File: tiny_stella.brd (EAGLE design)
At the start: 99.7 x 85.1 mm, 73 parts, among them SW1 RGT_DIFFICULTY, SW2 LFT_DIFFICULTY, SW3 ON/OFF, T1 2N3904, T2 PN3906, T3 PN3906, X1 SSW-112-02-G-Q

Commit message: labeled everything and started laying traces
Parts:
- S3, S4: device SparkFun-Switches:TACTILE_SWITCH_SMD_6.0X3.5MM -> SparkFun-Switches:TACTILE_SWITCH_PTH_6.0MM_KIT
- moved JP1 7.34 mm to (71.4, 64.9)
- moved R11 6.40 mm to (36.3, 38.4), flipped to the bottom, turned to 0 degrees
- moved R10 6.14 mm to (36.3, 36.1), flipped to the bottom, turned to 0 degrees
- moved C1 5.89 mm to (36.3, 33.8), flipped to the bottom
- moved R5 5.64 mm to (36.3, 31.5), flipped to the bottom
- moved R4 5.39 mm to (36.3, 29.2), flipped to the bottom
- moved R3 5.14 mm to (36.3, 26.9), flipped to the bottom, turned to 0 degrees
- moved R8 5.14 mm to (36.3, 24.4), flipped to the bottom, turned to 0 degrees
- moved R2 4.58 mm to (31.8, 26.9), flipped to the bottom, turned to 0 degrees
- moved R7 4.58 mm to (31.8, 24.4), flipped to the bottom, turned to 0 degrees
- moved R20 4.06 mm to (45.7, 10.2), flipped to the bottom, turned to 0 degrees
- moved SW1 3.87 mm to (56.9, 74.9), turned to 90 degrees
- moved SW2 3.87 mm to (56.9, 69.8), turned to 270 degrees
- moved R1 3.81 mm to (31.8, 19.3), flipped to the bottom, turned to 0 degrees
- moved R6 3.81 mm to (31.8, 16.8), flipped to the bottom, turned to 0 degrees
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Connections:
- net GND: now also S3.3, S4.3; no longer S3.2, S4.2
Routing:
- net N$8: track 0.00 -> 28.3 mm
- net N$17: track 0.00 -> 25.2 mm
- net N$25: track 0.00 -> 22.4 mm
- net +5V: track 0.00 -> 17.9 mm, vias 0 -> 2
- net N$14: track 0.00 -> 16.6 mm
- net N$4: track 0.00 -> 16.2 mm, vias 0 -> 1
- net N$5: track 0.00 -> 15.2 mm, vias 0 -> 1
- net N$16: track 0.00 -> 14.1 mm, vias 0 -> 2
- net N$3: track 0.00 -> 12.7 mm, vias 0 -> 1
- net N$15: track 0.00 -> 6.70 mm
- net N$13: track 0.00 -> 6.37 mm
- net N$2: track 0.00 -> 6.04 mm
- net N$1: track 0.00 -> 6.04 mm
- net N$6: track 0.00 -> 4.57 mm
- net N$24: track 0.00 -> 3.97 mm
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- added copper zone on layer 1, net GND
- added copper zone on layer 16, net GND
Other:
- board text added: "+5V"
- board text added: "A10"
- board text added: "A11"
- board text added: "A12"
- board text added: "A6"
- board text added: "A7"
- board text added: "A8"
- board text added: "A9"
- board text added: "AU1"
- board text added: "AU2"
- board text added: "AUDIO"
- board text added: "BLK"
- board text added: "BUTTONS"
- board text added: "BW/ COLOR"
- board text added: "CLK"
- board text added: "COL"
- board text added: "D1"
- board text added: "D2"
- board text added: "D3"
- board text added: "D4"
- board text added: "D5"
- board text added: "D6"
- board text added: "D7"
- board text added: "D8"
- board text added: "DATA BUS"
- board text added: "DEL"
- board text added: "IRQ"
- board text added: "LEFT FIRE"
- board text added: "LEFT PADDLE A"
- board text added: "LEFT PADDLE B"
- board text added: "LM0"
- board text added: "LM1"
- board text added: "LM2"
- board text added: "PADDLES"
- board text added: "PB2"
- board text added: "PHI0"
- board text added: "PHI2"
- board text added: "R/W"
- board text added: "RDY"
- board text added: "RES"
- board text added: "RIGHT FIRE"
- board text added: "RIGHT PADDLE A"
- board text added: "RIGHT PADDLE B"
- board text added: "SELECT"
- board text added: "SHORT T0 RESET"
- board text added: "START"
- board text added: "SYNC"
- board text added: "VIDEO"

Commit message: more traces
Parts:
- moved C10 81.3 mm to (73.4, 57.4), turned to 0 degrees
- moved C5 11.4 mm to (6.35, 32.8), turned to 90 degrees
- moved C9 9.15 mm to (28.2, 69.1), turned to 180 degrees
- moved R30 8.92 mm to (6.10, 51.3), turned to 270 degrees
- moved C14 5.47 mm to (40.4, 68.3), turned to 0 degrees
- moved R29 4.83 mm to (2.29, 46.7)
- moved T3 4.58 mm to (2.54, 42.4)
- moved C19 2.81 mm to (2.29, 51.3), turned to 90 degrees
- moved R15 2.79 mm to (3.05, 22.1)
- moved X1 1.52 mm to (53.0, 59.3)
- moved C8 0.25 mm to (24.1, 69.1), turned to 0 degrees
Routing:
- net A0: track 0.00 -> 58.5 mm
- net A1: track 0.00 -> 56.0 mm
- net A2: track 0.00 -> 53.5 mm, vias 0 -> 2
- net A3: track 0.00 -> 51.8 mm
- net RGT_JOY_UP: track 0.00 -> 48.6 mm
- net A4: track 0.00 -> 47.5 mm
- net RGT_JOY_DWN: track 0.00 -> 44.2 mm
- net A5: track 0.00 -> 41.0 mm
- net RGT_JOY_LFT: track 0.00 -> 40.5 mm
- net +5V: track 17.9 -> 58.3 mm
- net RGT_JOY_RGT: track 0.00 -> 38.1 mm
- net N$32: track 0.00 -> 33.4 mm
- net N$27: track 0.00 -> 16.3 mm
- net N$31: track 0.00 -> 13.7 mm
- net N$33: track 0.00 -> 11.6 mm, vias 0 -> 2
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
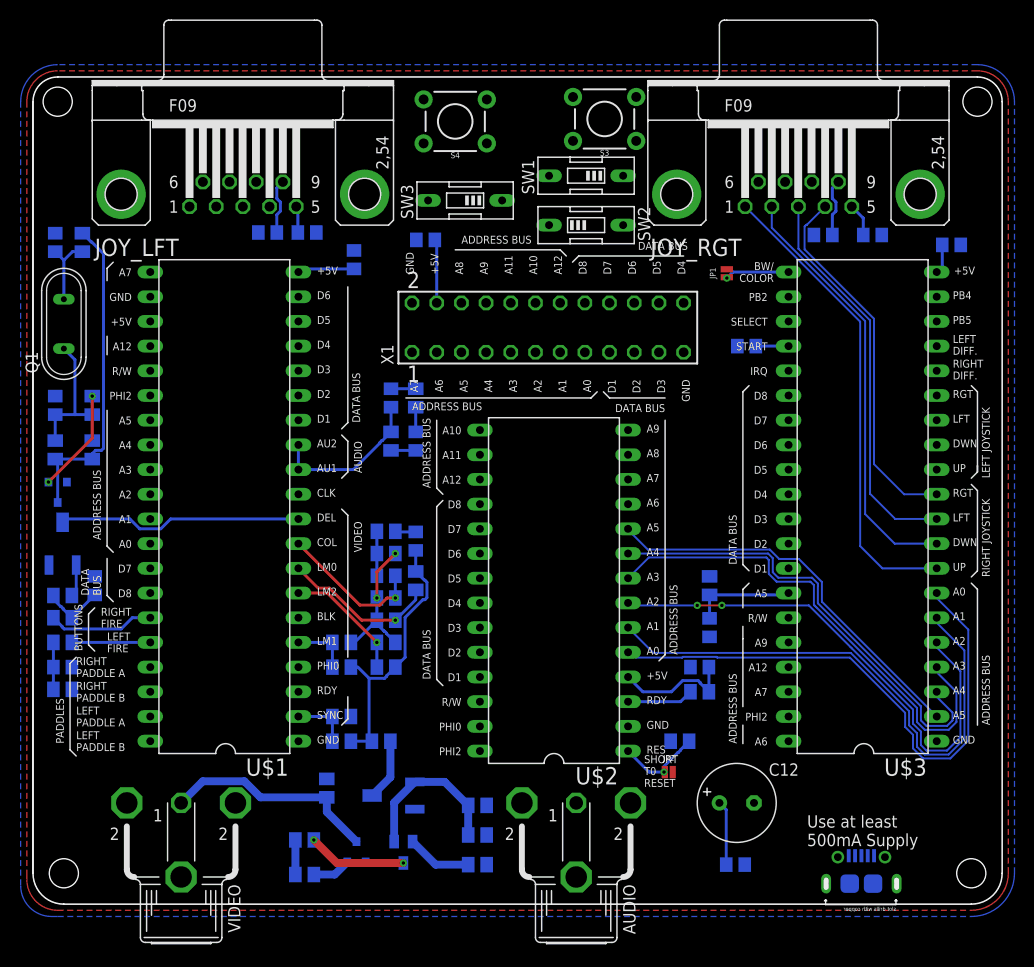
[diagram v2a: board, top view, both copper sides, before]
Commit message: added pausing circuitry
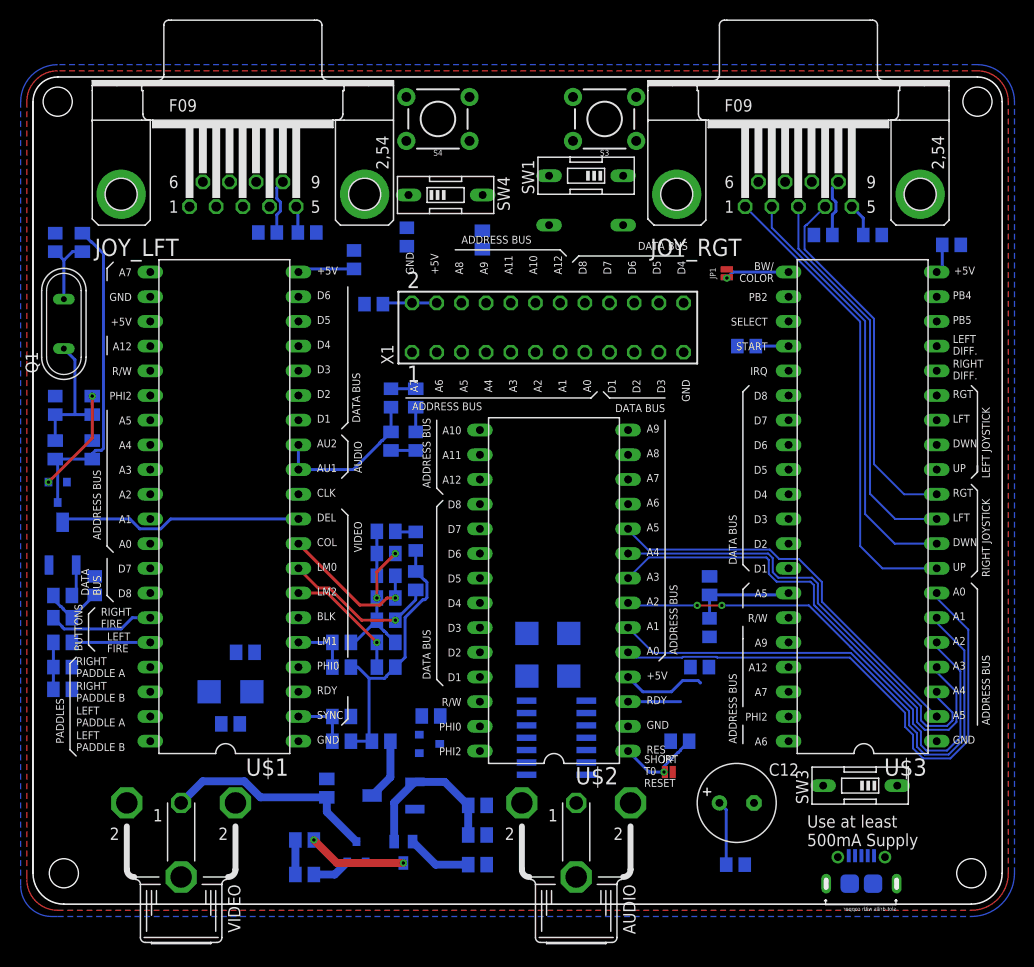
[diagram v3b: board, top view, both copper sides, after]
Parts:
- added C21: 100nF, resistor:C0805
- added D1, D2, D3: (no value), eagle-ltspice:DIODE_SMB
- added IC1: 74LS00D, 74xx-us:SO14
- added R32: 1.5k, resistor:M0805
- added R33, R34: 1k, resistor:M0805
- added SW4: ON/OFF, special:EDG-01
- added T4: PN3906, User-Submitted:SOT23-3
- R17: value 4.7k -> 1k
- moved SW3 72.6 mm to (85.1, 12.2)
- moved R17 27.7 mm to (40.9, 19.4), turned to 0 degrees
- moved C14 8.49 mm to (35.1, 61.7)
- moved S4 1.80 mm to (41.7, 80.8)
- flipped SW2 to the bottom
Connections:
- removed net RDY: R17.1, U$1.3, U$2.3
- new net CPU_RDY: IC1.11, U$2.3
- new net N$34: R17.1, T4.3
- new net N$35: IC1.12, IC1.13, IC1.5, IC1.8
- new net N$36: D3.A, IC1.2
- new net N$38: IC1.3, IC1.4
- new net N$39: D1.A, IC1.10, IC1.6
- new net N$40: D1.C, D2.C, IC1.1, IC1.9, R33.1
- new net P_SW: D3.C, R34.2, SW4.2, T4.1
- new net TIA_RDY: D2.A, R32.2, U$1.3
- new net VCC: IC1.14
- net +5V: now also R32.1, R34.1; no longer R17.2
- net GND: now also C21.2, IC1.7, R17.2, R33.2, SW4.1
- net N$13: now also T4.2
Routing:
- net RDY: track 6.84 -> 0.00 mm
- net CPU_RDY: track 0.00 -> 5.40 mm
- net +5V: track 58.3 -> 53.6 mm

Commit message: more routing
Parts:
- moved C14 10.2 mm to (42.3, 68.9)
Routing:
- net RGT_PADDLE_A: track 6.03 -> 156.8 mm, vias 0 -> 1
- net RGT_PADDLE_B: track 3.41 -> 153.3 mm, vias 0 -> 1
- net D5: track 0.00 -> 115.2 mm, vias 0 -> 1
- net A12: track 0.00 -> 111.2 mm, vias 0 -> 1
- net D4: track 0.00 -> 110.3 mm, vias 0 -> 3
- net D6: track 0.00 -> 110.3 mm, vias 0 -> 2
- net LFT_JOY_UP: track 0.00 -> 109.4 mm, vias 0 -> 1
- net D1: track 0.00 -> 107.1 mm, vias 0 -> 2
- net A1: track 56.0 -> 161.4 mm, vias 0 -> 1
- net D3: track 0.00 -> 103.5 mm, vias 0 -> 1
- net D2: track 0.00 -> 102.9 mm, vias 0 -> 3
- net D7: track 0.00 -> 101.4 mm, vias 0 -> 3
- net N$9: track 6.43 -> 106.8 mm, vias 0 -> 3
- net LFT_JOY_DWN: track 0.00 -> 99.9 mm, vias 0 -> 1
- net PHI_2: track 0.00 -> 99.4 mm
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
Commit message: even more routing
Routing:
- net +5V: track 55.7 -> 456.7 mm, vias 2 -> 23
- net R/W: track 45.1 -> 113.9 mm, vias 0 -> 8
- net P_SW: track 54.2 -> 93.3 mm, vias 2 -> 7
- net N$40: track 30.1 -> 67.7 mm, vias 2 -> 4
- net GND: track 0.00 -> 27.3 mm, vias 2 -> 3
- net N$27: track 16.3 -> 25.1 mm, vias 0 -> 2
- net VBUS: track 0.00 -> 8.20 mm
- net D3: track 103.5 -> 108.9 mm
- net N$13: track 6.37 -> 9.62 mm
- net D6: track 110.3 -> 113.3 mm
- net N$34: track 0.00 -> 2.89 mm
- net D5: track 115.2 -> 117.2 mm
- net D2: track 102.9 -> 104.7 mm
- net PHI_2: track 99.4 -> 100.6 mm
- net N$5: track 15.2 -> 16.4 mm
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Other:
- board text added: "CS1"

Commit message: even more routing
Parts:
- moved SW1 0.51 mm to (56.9, 74.4), turned to 270 degrees
- flipped SW2 to the top
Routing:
- net GND: track 27.3 -> 53.4 mm, vias 3 -> 5
- net +5V: track 456.7 -> 474.7 mm, vias 23 -> 22
- net N$22: track 50.3 -> 43.0 mm
- net N$21: track 47.5 -> 41.2 mm
- net R/W: track 113.9 -> 115.6 mm
- net N$33: track 11.6 -> 10.7 mm
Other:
- board text added: "Atari Television Interface Adapter"
- board text added: "MOS Technologies 6507 Microprocessor"
- board text added: "MOS Technologies 6532 RIOT Chip"
- board text added: "This chip serves two functions; It holds the system's 128 bytes of RAM and gives the CPU more I/O so it can connect with all the controllers and difficulty switches."
- board text added: "This chip was custom manufactured by Atari and is responsible for drawing everything on the screen, producing sound, and reading some controller input. It's considered by many to be the soul of the system"
- board text added: "This was a cost reduced version of the very popular 6502 processor"

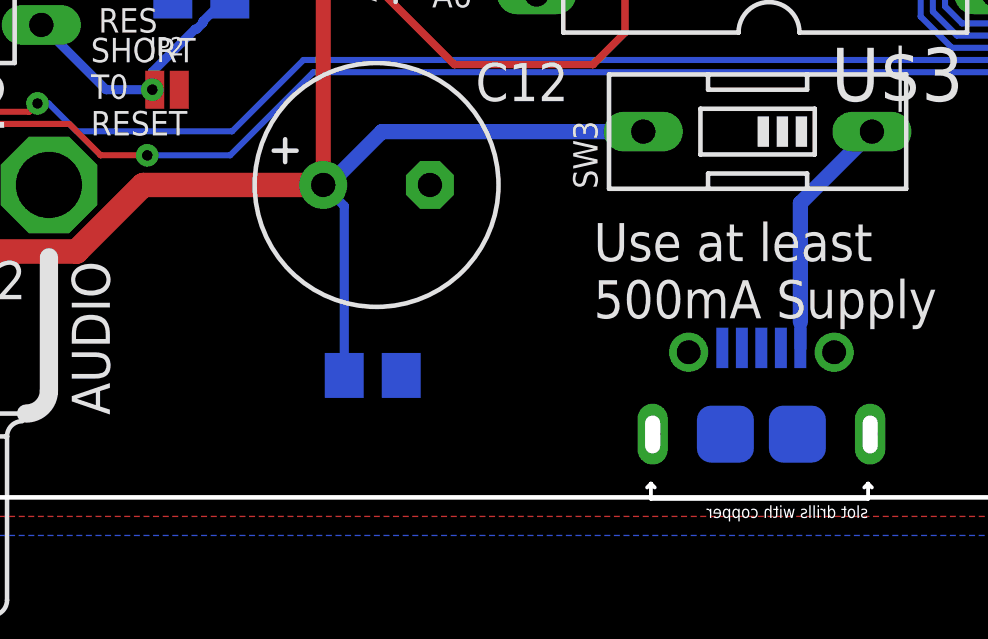
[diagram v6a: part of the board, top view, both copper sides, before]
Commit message: added breakout for the power
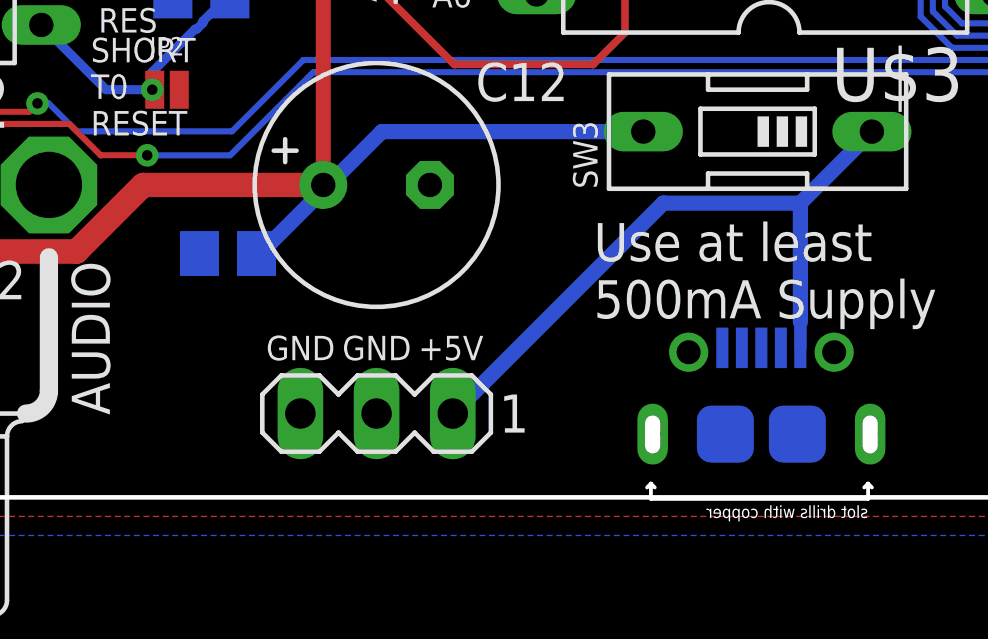
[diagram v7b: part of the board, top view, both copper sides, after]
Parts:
- added SV1: (no value), con-lstb:MA03-1
- moved C13 6.31 mm to (67.4, 8.13), turned to 0 degrees
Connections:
- net GND: now also SV1.2, SV1.3
- net VBUS: now also SV1.1
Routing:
- net VBUS: track 8.20 -> 22.7 mm
- net +5V: track 474.7 -> 471.5 mm
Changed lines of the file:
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@@
 drawing everything on the screen, producing sound, and reading some
 controller input. It's considered by many to be the soul of the system</text>
+<text x="73.787" y="4.572" size="0.8128" layer="25" font="vector" ratio="20">+5V</text>
+<text x="75.819" y="4.572" size="0.8128" layer="26" font="vector" ratio="20" rot="MR0">+5V</text>
+<text x="71.247" y="4.572" size="0.8128" layer="25" font="vector" ratio="20">GND</text>
+<text x="73.279" y="4.572" size="0.8128" layer="26" font="vector" ratio="20" rot="MR0">GND</text>
+<text x="70.739" y="4.572" size="0.8128" layer="26" font="vector" ratio="20" rot="MR0">GND</text>
+<text x="68.707" y="4.572" size="0.8128" layer="25" font="vector" ratio="20">GND</text>
 </plain>
 <attributes>
@@
 <element name="USB1" library="Seeed-Connector" library_urn="urn:adsk.eagle:library:478" package="MICRO-USB5+6P-SMD-0.65-AB" package3d_urn="urn:adsk.eagle:package:33147/1" value="ZX62-B-5PA" x="85.217" y="2.1082" smashed="yes" rot="MR0">
 <attribute name="MPN" value="ZX62-B-5PA" x="85.217" y="2.1082" size="1.778" layer="28" rot="MR0" display="off"/>
-<attribute name="NAME" x="89.027" y="6.35" size="1.27" layer="26" font="vector" ratio="20" rot="MR0"/>
+<attribute name="NAME" x="91.186" y="4.953" size="1.27" layer="26" font="vector" ratio="20" rot="MR270"/>
 </element>
 <element name="C12" library="resistor" library_urn="urn:adsk.eagle:library:348" package="E3,5-8" package3d_urn="urn:adsk.eagle:package:25842/1" value="1F" x="72.39" y="10.414"/>
-<element name="C13" library="resistor" library_urn="urn:adsk.eagle:library:348" package="C0805" package3d_urn="urn:adsk.eagle:package:26137/1" value="100nF" x="72.263" y="4.064" smashed="yes" rot="MR180">
-<attribute name="NAME" x="69.342" y="2.921" size="0.8128" layer="26" rot="MR90"/>
-<attribute name="VALUE" x="70.993" y="6.604" size="1.27" layer="28" rot="MR180"/>
+<element name="C13" library="resistor" library_urn="urn:adsk.eagle:library:348" package="C0805" package3d_urn="urn:adsk.eagle:package:26137/1" value="100nF" x="67.437" y="8.128" smashed="yes" rot="MR0">
+<attribute name="NAME" x="70.358" y="9.271" size="0.8128" layer="26" rot="MR270"/>
+<attribute name="VALUE" x="68.707" y="5.588" size="1.27" layer="28" rot="MR0"/>
 </element>
 <element name="C14" library="resistor" library_urn="urn:adsk.eagle:library:348" package="C0805" package3d_urn="urn:adsk.eagle:package:26137/1" value="100nF" x="42.3164" y="68.8848" smashed="yes" rot="MR0">
@@
 <attribute name="PROD_ID" value="TRANS-08052" x="40.7416" y="16.4846" size="1.778" layer="28" rot="MR90" display="off"/>
 <attribute name="VALUE" x="40.5511" y="15.4686" size="0.4064" layer="28" rot="MR90"/>
+</element>
+<element name="SV1" library="con-lstb" library_urn="urn:adsk.eagle:library:162" package="MA03-1" package3d_urn="urn:adsk.eagle:package:8339/1" value="" x="72.39" y="2.794" smashed="yes" rot="R180">
+<attribute name="MF" value="" x="72.39" y="2.794" size="1.778" layer="27" rot="R180" display="off"/>
+<attribute name="MPN" value="" x="72.39" y="2.794" size="1.778" layer="27" rot="R180" display="off"/>
+<attribute name="OC_FARNELL" value="unknown" x="72.39" y="2.794" size="1.778" layer="27" rot="R180" display="off"/>
+<attribute name="OC_NEWARK" value="unknown" x="72.39" y="2.794" size="1.778" layer="27" rot="R180" display="off"/>
+<attribute name="VALUE" x="76.2" y="5.715" size="1.27" layer="27" ratio="10" rot="R180"/>
 </element>
 </elements>
@@
 <wire x1="27.625" y1="65.344" x2="33.02" y2="65.344" width="0.3048" layer="16"/>
 <wire x1="39.37" y1="46.675" x2="36.83" y2="46.675" width="0.3048" layer="16"/>
-<wire x1="71.313" y1="4.064" x2="71.313" y2="9.713" width="0.3048" layer="16"/>
-<wire x1="71.313" y1="9.713" x2="70.7009" y2="10.3251" width="0.3048" layer="16"/>
+<wire x1="68.387" y1="8.067" x2="68.387" y2="8.128" width="0.3048" layer="16"/>
+<wire x1="68.4149" y1="8.0391" x2="68.387" y2="8.067" width="0.3048" layer="16"/>
 <wire x1="70.7009" y1="10.3251" x2="70.612" y2="10.414" width="0.3048" layer="16"/>
 <wire x1="93.538" y1="67.818" x2="93.538" y2="65.598" width="0.3048" layer="16"/>
@@
 <wire x1="13.716" y1="29.874325" x2="13.716" y2="26.513675" width="0.254" layer="16"/>
 <wire x1="43.2664" y1="68.8848" x2="41.529" y2="67.1474" width="0.254" layer="16"/>
+<wire x1="70.7009" y1="10.3251" x2="68.4149" y2="8.0391" width="0.508" layer="16"/>
 </signal>
 <signal name="N$6">
@@
 <wire x1="1.778" y1="34.798" x2="1.778" y2="35.052" width="0.2032" layer="1"/>
 <wire x1="1.778" y1="35.052" x2="1.778" y2="34.798" width="0.2032" layer="1"/>
+<contactref element="SV1" pad="2"/>
+<contactref element="SV1" pad="3"/>
 </signal>
 <signal name="N$9">
@@
 <wire x1="86.517" y1="9.809" x2="88.9" y2="12.192" width="0.508" layer="16"/>
 <wire x1="86.517" y1="4.9832" x2="86.517" y2="5.842" width="0.4064" layer="16"/>
+<contactref element="SV1" pad="1"/>
+<wire x1="74.93" y1="2.794" x2="81.945" y2="9.809" width="0.508" layer="16"/>
+<wire x1="81.945" y1="9.809" x2="86.517" y2="9.809" width="0.508" layer="16"/>
 </signal>
 <signal name="N$29">
